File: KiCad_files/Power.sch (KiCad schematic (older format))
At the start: 101 parts, among them J2 PCIe_6_Pin_Power, Q1 Q_NMOS_DGS, Q2 Q_PMOS_DGS, U1 XC7A35T_CSG325, U13 LM2676, U2 MAX15027, U3 PI3420, U4 PI3421, U5 PI3420

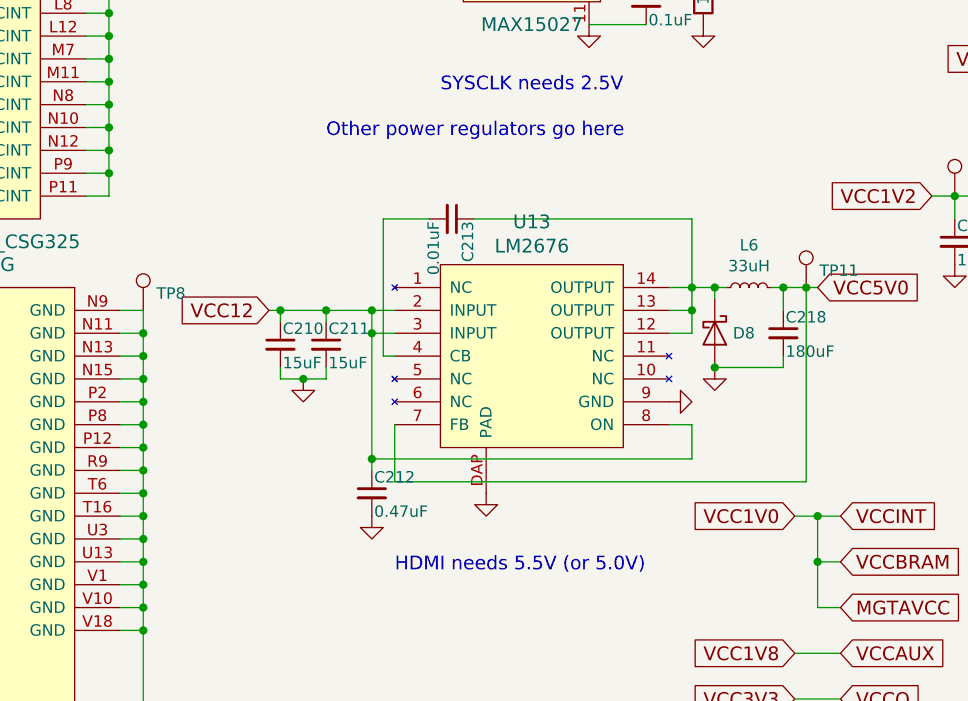
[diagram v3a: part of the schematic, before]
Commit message: Fixed LM2676
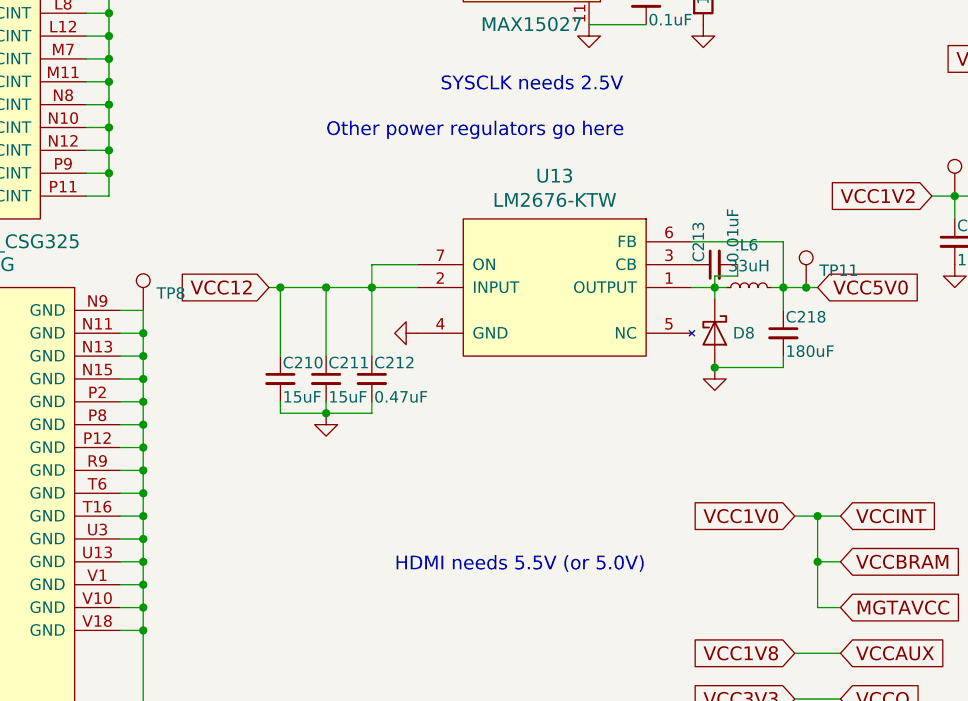
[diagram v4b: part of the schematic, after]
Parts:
- removed U13: LM2676, TO_SOT_Packages_SMD:TO-263-7_TabPin8, symbol custom:LM2676
- added U13: LM2676-KTW, symbol custom:LM2676-KTW
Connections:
- net GND: now also U13.4 (GND)
- net PCIe_12V: now also U13.2 (INPUT), U13.7 (ON)
- net VCC5V0: now also U13.6 (FB)
- net at D8.1 (K), L6.1: now also C213.2, U13.1 (OUTPUT); no longer C213.1
- new net: C213.1, U13.3 (CB)
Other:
- moved on the sheet: C210, C211, C212, C213
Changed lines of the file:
@@
 Wire Wire Line
 	9700 5950 9850 5950
-$Comp
-L custom:LM2676 U13
-U 1 1 5C81CD56
-P 4900 5700
-F 0 "U13" H 4900 6487 60  0000 C CNN
-F 1 "LM2676" H 4900 6381 60  0000 C CNN
-F 2 "TO_SOT_Packages_SMD:TO-263-7_TabPin8" H 4900 5850 60  0001 C CNN
-F 3 "" H 4900 5850 60  0001 C CNN
-	1    4900 5700
-	1    0    0    -1
-$EndComp
-$Comp
-L power:GND #PWR0133
-U 1 1 5C81D209
-P 5500 5700
-F 0 "#PWR0133" H 5500 5450 50  0001 C CNN
-F 1 "GND" H 5500 5550 50  0001 C CNN
-F 2 "" H 5500 5700 50  0001 C CNN
-F 3 "" H 5500 5700 50  0001 C CNN
-	1    5500 5700
-	0    -1   -1   0
-$EndComp
-Wire Wire Line
-	4200 5950 4200 5400
-Wire Wire Line
-	4200 5300 4300 5300
-Wire Wire Line
-	4300 5400 4200 5400
-Connection ~ 4200 5400
-Wire Wire Line
-	4200 5400 4200 5300
-Wire Wire Line
-	5500 5800 5600 5800
-Wire Wire Line
-	5600 5800 5600 5950
-Wire Wire Line
-	4200 5950 5600 5950
-Text GLabel 3750 5300 0    60   Input ~ 0
+Text GLabel 3750 5200 0    60   Input ~ 0
 VCC12
-Connection ~ 4200 5300
 Text GLabel 6150 5200 2    60   Input ~ 0
 VCC5V0
-Wire Wire Line
-	5500 5200 5600 5200
-Wire Wire Line
-	5600 5200 5600 5300
-Wire Wire Line
-	5600 5400 5500 5400
-Connection ~ 5600 5200
-Wire Wire Line
-	5600 5200 5700 5200
-Wire Wire Line
-	5500 5300 5600 5300
-Connection ~ 5600 5300
-Wire Wire Line
-	5600 5300 5600 5400
 $Comp
 L Device:C_Small C210
 U 1 1 5C7B6C9B
-P 3800 5450
-F 0 "C210" H 3810 5520 50  0000 L CNN
-F 1 "15uF" H 3810 5370 50  0000 L CNN
-F 2 "Capacitors_SMD:C_1210" H 3800 5450 50  0001 C CNN
-F 3 "" H 3800 5450 50  0001 C CNN
-	1    3800 5450
+P 3800 5600
+F 0 "C210" H 3810 5670 50  0000 L CNN
+F 1 "15uF" H 3810 5520 50  0000 L CNN
+F 2 "Capacitors_SMD:C_1210" H 3800 5600 50  0001 C CNN
+F 3 "" H 3800 5600 50  0001 C CNN
+	1    3800 5600
 	1    0    0    -1
 $EndComp
@@
 L Device:C_Small C211
 U 1 1 5C7B733D
-P 4000 5450
-F 0 "C211" H 4010 5520 50  0000 L CNN
-F 1 "15uF" H 4010 5370 50  0000 L CNN
-F 2 "Capacitors_SMD:C_1210" H 4000 5450 50  0001 C CNN
-F 3 "" H 4000 5450 50  0001 C CNN
-	1    4000 5450
+P 4000 5600
+F 0 "C211" H 4010 5670 50  0000 L CNN
+F 1 "15uF" H 4010 5520 50  0000 L CNN
+F 2 "Capacitors_SMD:C_1210" H 4000 5600 50  0001 C CNN
+F 3 "" H 4000 5600 50  0001 C CNN
+	1    4000 5600
 	1    0    0    -1
 $EndComp
@@
 L Device:C_Small C212
 U 1 1 5C7B740B
-P 4200 6100
-F 0 "C212" H 4210 6170 50  0000 L CNN
-F 1 "0.47uF" H 4210 6020 50  0000 L CNN
-F 2 "Capacitors_SMD:C_0402" H 4200 6100 50  0001 C CNN
-F 3 "" H 4200 6100 50  0001 C CNN
-	1    4200 6100
-	1    0    0    -1
-$EndComp
-$Comp
-L power:GND #PWR0132
-U 1 1 5C7B75E7
-P 4200 6200
-F 0 "#PWR0132" H 4200 5950 50  0001 C CNN
-F 1 "GND" H 4200 6050 50  0001 C CNN
-F 2 "" H 4200 6200 50  0001 C CNN
-F 3 "" H 4200 6200 50  0001 C CNN
-	1    4200 6200
-	1    0    0    -1
-$EndComp
-Wire Wire Line
-	4200 6000 4200 5950
-Connection ~ 4200 5950
+P 4200 5600
+F 0 "C212" H 4210 5670 50  0000 L CNN
+F 1 "0.47uF" H 4210 5520 50  0000 L CNN
+F 2 "Capacitors_SMD:C_0402" H 4200 5600 50  0001 C CNN
+F 3 "" H 4200 5600 50  0001 C CNN
+	1    4200 5600
+	1    0    0    -1
+$EndComp
 $Comp
 L power:GND #PWR0131
 U 1 1 5C813FA2
-P 3900 5600
-F 0 "#PWR0131" H 3900 5350 50  0001 C CNN
-F 1 "GND" H 3900 5450 50  0001 C CNN
-F 2 "" H 3900 5600 50  0001 C CNN
-F 3 "" H 3900 5600 50  0001 C CNN
-	1    3900 5600
-	1    0    0    -1
-$EndComp
-Wire Wire Line
-	4000 5350 4000 5300
-Connection ~ 4000 5300
-Wire Wire Line
-	4000 5300 4200 5300
-Wire Wire Line
-	4000 5550 4000 5600
-Wire Wire Line
-	4000 5600 3900 5600
-Wire Wire Line
-	3750 5300 3800 5300
-Wire Wire Line
-	3800 5550 3800 5600
-Wire Wire Line
-	3800 5600 3900 5600
-Connection ~ 3900 5600
-Wire Wire Line
-	3800 5350 3800 5300
-Connection ~ 3800 5300
-Wire Wire Line
-	3800 5300 4000 5300
+P 4000 5750
+F 0 "#PWR0131" H 4000 5500 50  0001 C CNN
+F 1 "GND" H 4000 5600 50  0001 C CNN
+F 2 "" H 4000 5750 50  0001 C CNN
+F 3 "" H 4000 5750 50  0001 C CNN
+	1    4000 5750
+	1    0    0    -1
+$EndComp
+Connection ~ 4000 5200
+Wire Wire Line
+	4000 5700 4000 5750
+Wire Wire Line
+	3750 5200 3800 5200
+Wire Wire Line
+	3800 5700 3800 5750
+Connection ~ 3800 5200
+Wire Wire Line
+	3800 5200 4000 5200
 $Comp
 L Device:C_Small C213
 U 1 1 5C963D14
-P 4550 4900
-F 0 "C213" H 4560 4970 50  0000 L CNN
-F 1 "0.01uF" H 4560 4820 50  0000 L CNN
-F 2 "Capacitors_SMD:C_0201" H 4550 4900 50  0001 C CNN
-F 3 "" H 4550 4900 50  0001 C CNN
-	1    4550 4900
-	0    1    1    0
-$EndComp
-Wire Wire Line
-	4300 5500 4250 5500
-Wire Wire Line
-	4250 5500 4250 4900
-Wire Wire Line
-	4250 4900 4450 4900
-Wire Wire Line
-	4650 4900 5600 4900
-Wire Wire Line
-	5600 4900 5600 5200
+P 5700 5100
+F 0 "C213" H 5710 5170 50  0000 L CNN
+F 1 "0.01uF" H 5710 5020 50  0000 L CNN
+F 2 "Capacitors_SMD:C_0201" H 5700 5100 50  0001 C CNN
+F 3 "" H 5700 5100 50  0001 C CNN
+	1    5700 5100
+	0    -1   -1   0
+$EndComp
 $Comp
 L Device:D_Schottky D8
@@
 Wire Wire Line
 	5750 5200 5700 5200
-Connection ~ 5700 5200
 Wire Wire Line
 	5950 5200 6000 5200
@@
 Wire Wire Line
 	6000 5200 6100 5200
-Wire Wire Line
-	6100 5200 6100 6050
-Wire Wire Line
-	6100 6050 4300 6050
-Wire Wire Line
-	4300 6050 4300 5800
 Connection ~ 6100 5200
 Wire Wire Line
@@
 L power:GND #PWR0142
 U 1 1 5C7CA813
-P 4700 6100
-F 0 "#PWR0142" H 4700 5850 50  0001 C CNN
-F 1 "GND" H 4700 5950 50  0001 C CNN
-F 2 "" H 4700 6100 50  0001 C CNN
-F 3 "" H 4700 6100 50  0001 C CNN
-	1    4700 6100
-	1    0    0    -1
+P 4400 5400
+F 0 "#PWR0142" H 4400 5150 50  0001 C CNN
+F 1 "GND" H 4400 5250 50  0001 C CNN
+F 2 "" H 4400 5400 50  0001 C CNN
+F 3 "" H 4400 5400 50  0001 C CNN
+	1    4400 5400
+	0    1    1    0
 $EndComp
 Wire Wire Line
 	10000 1100 9900 1100
 NoConn ~ 9900 1200
+$Comp
+L custom:LM2676-KTW U13
+U 1 1 5C7A9014
+P 5000 5300
+F 0 "U13" H 5000 5887 60  0000 C CNN
+F 1 "LM2676-KTW" H 5000 5781 60  0000 C CNN
+F 2 "" H 5000 5450 60  0001 C CNN
+F 3 "" H 5000 5450 60  0001 C CNN
+	1    5000 5300
+	1    0    0    -1
+$EndComp
+Wire Wire Line
+	5600 5200 5700 5200
+Connection ~ 5700 5200
+Wire Wire Line
+	5800 5100 5800 5150
+Wire Wire Line
+	5800 5150 5700 5150
+Wire Wire Line
+	5700 5150 5700 5200
+Wire Wire Line
+	5600 5000 6000 5000
+Wire Wire Line
+	6000 5000 6000 5200
+Wire Wire Line
+	3800 5750 4000 5750
+Wire Wire Line
+	4000 5750 4200 5750
+Connection ~ 4000 5750
+Wire Wire Line
+	4200 5700 4200 5750
+Wire Wire Line
+	4000 5200 4000 5500
+Wire Wire Line
+	3800 5200 3800 5500
+Wire Wire Line
+	4000 5200 4200 5200
+Wire Wire Line
+	4200 5100 4200 5200
+Wire Wire Line
+	4200 5100 4400 5100
+Connection ~ 4200 5200
+Wire Wire Line
+	4200 5200 4400 5200
+Wire Wire Line
+	4200 5500 4200 5200
 $EndSCHEMATC

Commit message: Should've been part of previous commit
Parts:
- U13: footprint (none) -> TO_SOT_Packages_SMD:TO-263-7_TabPin4
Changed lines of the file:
@@
 F 0 "U13" H 5000 5887 60  0000 C CNN
 F 1 "LM2676-KTW" H 5000 5781 60  0000 C CNN
-F 2 "" H 5000 5450 60  0001 C CNN
+F 2 "TO_SOT_Packages_SMD:TO-263-7_TabPin4" H 5000 5450 60  0001 C CNN
 F 3 "" H 5000 5450 60  0001 C CNN
 	1    5000 5300

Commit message: LGA-123 Drawn and added
PI3420 will come from Mouser...
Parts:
- U3, U4, U5: footprint (none) -> custom:LGA-123_10x14mm_Pitch1.0mm
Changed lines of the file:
@@
 F 0 "U3" H 9400 1800 60  0000 C CNN
 F 1 "PI3420" H 9400 700 60  0000 C CNN
-F 2 "" H 9300 1700 60  0001 C CNN
+F 2 "custom:LGA-123_10x14mm_Pitch1.0mm" H 9300 1700 60  0001 C CNN
 F 3 "" H 9300 1700 60  0001 C CNN
 	1    9400 1250
@@
 F 0 "U4" H 9400 3400 60  0000 C CNN
 F 1 "PI3421" H 9400 2300 60  0000 C CNN
-F 2 "" H 9300 3300 60  0001 C CNN
+F 2 "custom:LGA-123_10x14mm_Pitch1.0mm" H 9300 3300 60  0001 C CNN
 F 3 "" H 9300 3300 60  0001 C CNN
 	1    9400 2850
@@
 F 0 "U5" H 9400 5000 60  0000 C CNN
 F 1 "PI3420" H 9400 3900 60  0000 C CNN
-F 2 "" H 9300 4900 60  0001 C CNN
+F 2 "custom:LGA-123_10x14mm_Pitch1.0mm" H 9300 4900 60  0001 C CNN
 F 3 "" H 9300 4900 60  0001 C CNN
 	1    9400 4450

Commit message: Drew some more footprints
BTW another DRC error popped up since I2C level shifter now uses VCC5V0
TODO:
FPGA footprint + Inductors and FETs
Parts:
- U2: footprint (none) -> custom:TDFN-10_3x3mm_Pitch0.5mm
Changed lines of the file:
@@
 F 0 "U2" H 4900 4000 60  0000 C CNN
 F 1 "MAX15027" H 4900 3250 60  0000 C CNN
-F 2 "" H 4900 3450 60  0001 C CNN
+F 2 "custom:TDFN-10_3x3mm_Pitch0.5mm" H 4900 3450 60  0001 C CNN
 F 3 "" H 4900 3450 60  0001 C CNN
 	1    4900 3650

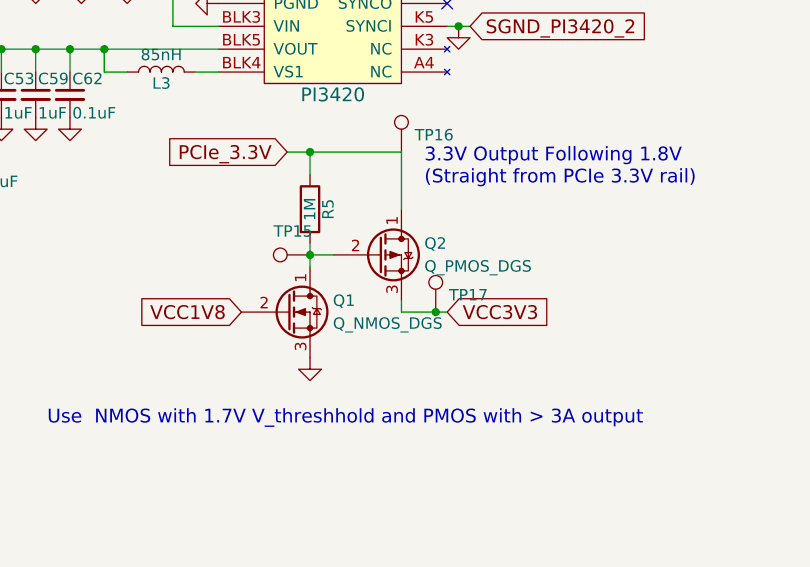
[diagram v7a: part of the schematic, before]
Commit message: Inductors and FETs footprints
TODO:
FPGA and HDMI foorprints
Layout
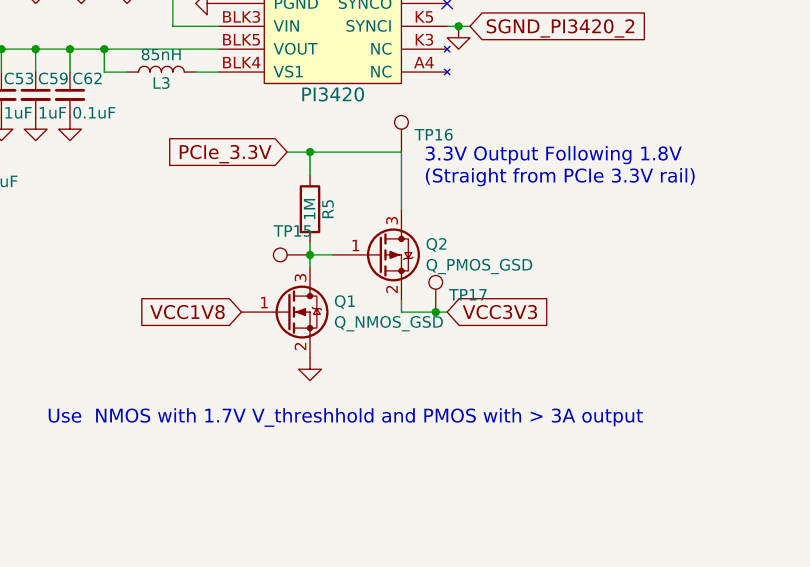
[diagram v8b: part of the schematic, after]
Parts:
- removed Q1: Q_NMOS_DGS, symbol Device:Q_NMOS_DGS
- removed Q2: Q_PMOS_DGS, symbol Device:Q_PMOS_DGS
- added Q1: Q_NMOS_GSD, TO_SOT_Packages_SMD:SOT-23, symbol Device:Q_NMOS_GSD
- added Q2: Q_PMOS_GSD, TO_SOT_Packages_SMD:SOT-23, symbol Device:Q_PMOS_GSD
- L1, L2, L3: footprint (none) -> Inductors_SMD:L_1210
- L6: footprint (none) -> Inductors_SMD:L_0805
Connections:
- net GND: now also Q1.2 (S)
- net PCIe_3.3V: now also Q2.3 (D)
- net VCC1V8: now also Q1.1 (G)
- net VCC3V3: now also Q2.2 (S)
- net at R5.2, TP15.1: now also Q1.3 (D), Q2.1 (G)
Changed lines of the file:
@@
 F 0 "L1" V 8600 1700 50  0000 C CNN
 F 1 "85nH" V 8725 1700 50  0000 C CNN
-F 2 "" H 8650 1700 50  0001 C CNN
+F 2 "Inductors_SMD:L_1210" H 8650 1700 50  0001 C CNN
 F 3 "" H 8650 1700 50  0001 C CNN
 	1    8650 1700
@@
 F 0 "L2" V 8600 3300 50  0000 C CNN
 F 1 "125nH" V 8725 3300 50  0000 C CNN
-F 2 "" H 8650 3300 50  0001 C CNN
+F 2 "Inductors_SMD:L_1210" H 8650 3300 50  0001 C CNN
 F 3 "" H 8650 3300 50  0001 C CNN
 	1    8650 3300
@@
 F 0 "L3" V 8600 4900 50  0000 C CNN
 F 1 "85nH" V 8725 4900 50  0000 C CNN
-F 2 "" H 8650 4900 50  0001 C CNN
+F 2 "Inductors_SMD:L_1210" H 8650 4900 50  0001 C CNN
 F 3 "" H 8650 4900 50  0001 C CNN
 	1    8650 4900
@@
 Text GLabel 10400 4500 2    60   Input ~ 0
 SGND_PI3420_2
-$Comp
-L Device:Q_NMOS_DGS Q1
-U 1 1 5C06597B
-P 9200 5950
-F 0 "Q1" H 9400 6000 50  0000 L CNN
-F 1 "Q_NMOS_DGS" H 9400 5900 50  0000 L CNN
-F 2 "" H 9400 6050 50  0001 C CNN
-F 3 "" H 9200 5950 50  0001 C CNN
-	1    9200 5950
-	1    0    0    -1
-$EndComp
 Text GLabel 9200 5250 0    60   Input ~ 0
 PCIe_3.3V
-$Comp
-L Device:Q_PMOS_DGS Q2
-U 1 1 5C0668D3
-P 9600 5700
-F 0 "Q2" H 9800 5750 50  0000 L CNN
-F 1 "Q_PMOS_DGS" H 9800 5650 50  0000 L CNN
-F 2 "" H 9800 5800 50  0001 C CNN
-F 3 "" H 9600 5700 50  0001 C CNN
-	1    9600 5700
-	1    0    0    -1
-$EndComp
 $Comp
 L Device:R R5
@@
 F 0 "L6" V 6035 5200 50  0000 C CNN
 F 1 "33uH" V 5944 5200 50  0000 C CNN
-F 2 "" H 5850 5200 50  0001 C CNN
+F 2 "Inductors_SMD:L_0805" H 5850 5200 50  0001 C CNN
 F 3 "~" H 5850 5200 50  0001 C CNN
 	1    5850 5200
@@
 Wire Wire Line
 	4200 5500 4200 5200
+$Comp
+L Device:Q_PMOS_GSD Q2
+U 1 1 5CC41EDF
+P 9600 5700
+F 0 "Q2" H 9806 5746 50  0000 L CNN
+F 1 "Q_PMOS_GSD" H 9806 5655 50  0000 L CNN
+F 2 "TO_SOT_Packages_SMD:SOT-23" H 9800 5800 50  0001 C CNN
+F 3 "~" H 9600 5700 50  0001 C CNN
+	1    9600 5700
+	1    0    0    -1
+$EndComp
+$Comp
+L Device:Q_NMOS_GSD Q1
+U 1 1 5CC44778
+P 9200 5950
+F 0 "Q1" H 9405 5996 50  0000 L CNN
+F 1 "Q_NMOS_GSD" H 9405 5905 50  0000 L CNN
+F 2 "TO_SOT_Packages_SMD:SOT-23" H 9400 6050 50  0001 C CNN
+F 3 "~" H 9200 5950 50  0001 C CNN
+	1    9200 5950
+	1    0    0    -1
+$EndComp
 $EndSCHEMATC
